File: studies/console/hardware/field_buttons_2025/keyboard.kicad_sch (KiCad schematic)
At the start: 69 parts, among them J1 Conn_02x12_Counter_Clockwise, SW1 SW_Push, SW10 SW_Push, SW11 SW_Push, SW12 SW_Push, SW13 SW_Push, SW14 SW_Push, SW15 SW_Push, SW16 SW_Push, SW17 SW_Push, SW18 SW_Push, SW19 SW_Push, SW2 SW_Push, SW20 SW_Push, SW21 SW_Push, SW22 SW_Push, SW23 SW_Push, SW24 SW_Push, SW25 SW_Push, SW26 SW_Push, SW27 SW_Push, SW28 SW_Push, SW29 SW_Push, SW3 SW_Push, SW30 SW_Push, SW31 SW_Push, SW32 SW_Push, SW4 SW_Push, SW5 SW_Push, SW6 SW_Push, SW7 SW_Push, SW8 SW_Push, SW9 SW_Push

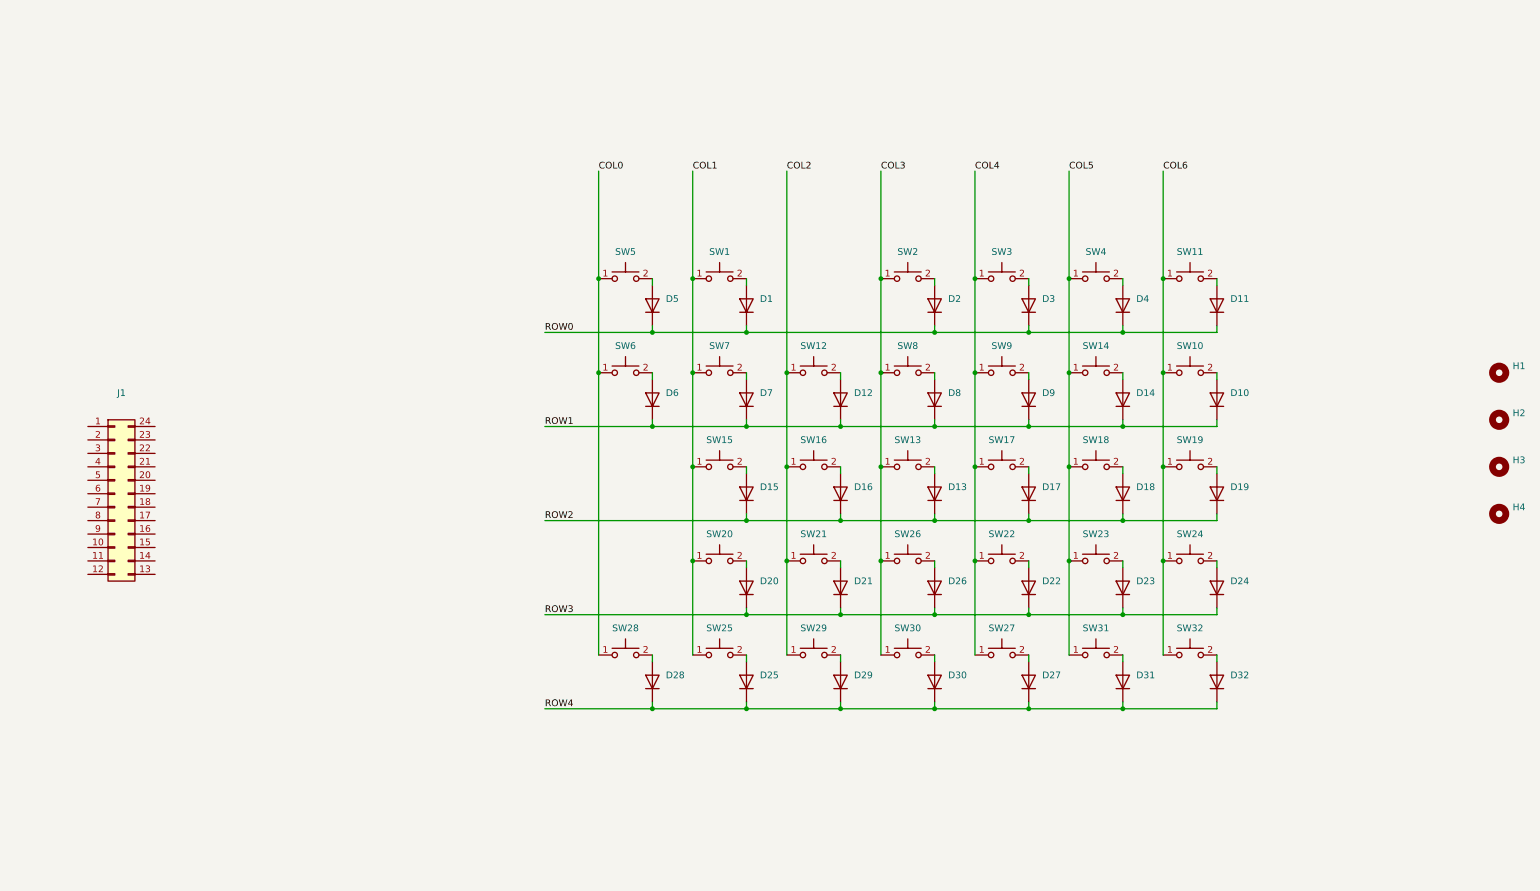
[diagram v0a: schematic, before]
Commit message: i added microcontroller tracks and code
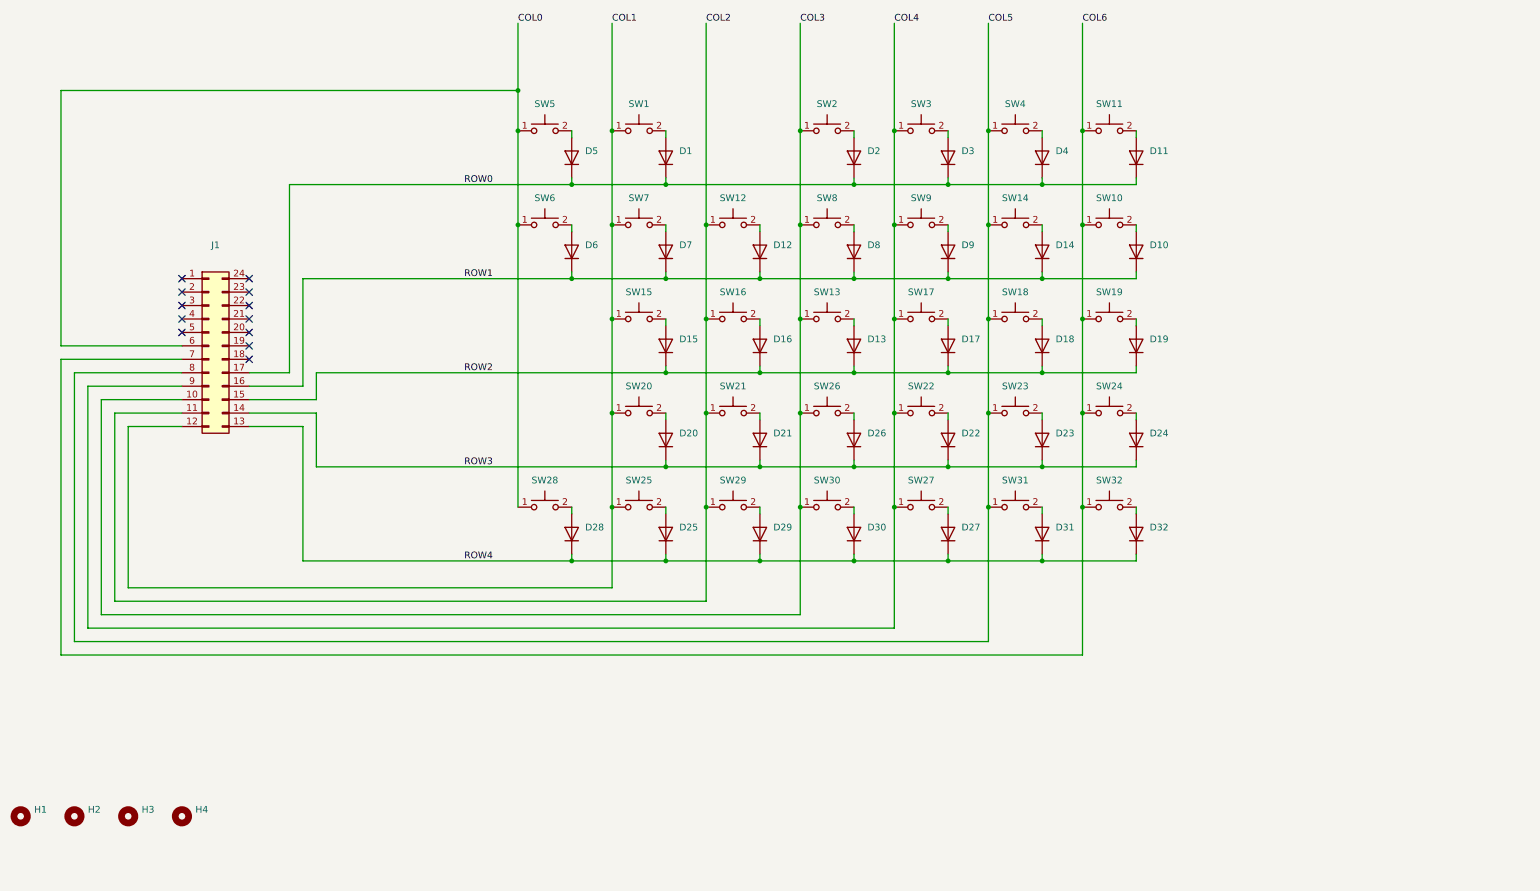
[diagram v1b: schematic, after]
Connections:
- net COL0: now also J1.6 (Pin_6)
- net COL1: now also J1.12 (Pin_12)
- net COL2: now also J1.11 (Pin_11)
- net COL3: now also J1.10 (Pin_10)
- net COL4: now also J1.9 (Pin_9)
- net COL5: now also J1.8 (Pin_8)
- net COL6: now also J1.7 (Pin_7)
- net ROW0: now also J1.17 (Pin_17)
- net ROW1: now also J1.16 (Pin_16)
- net ROW2: now also J1.15 (Pin_15)
- net ROW3: now also J1.14 (Pin_14)
- net ROW4: now also J1.13 (Pin_13)
- no-connect marks 0 -> 12
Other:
- moved on the sheet: D1, D10, D11, D12, D13, D14, D15, D16, D17, D18, D19, D2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

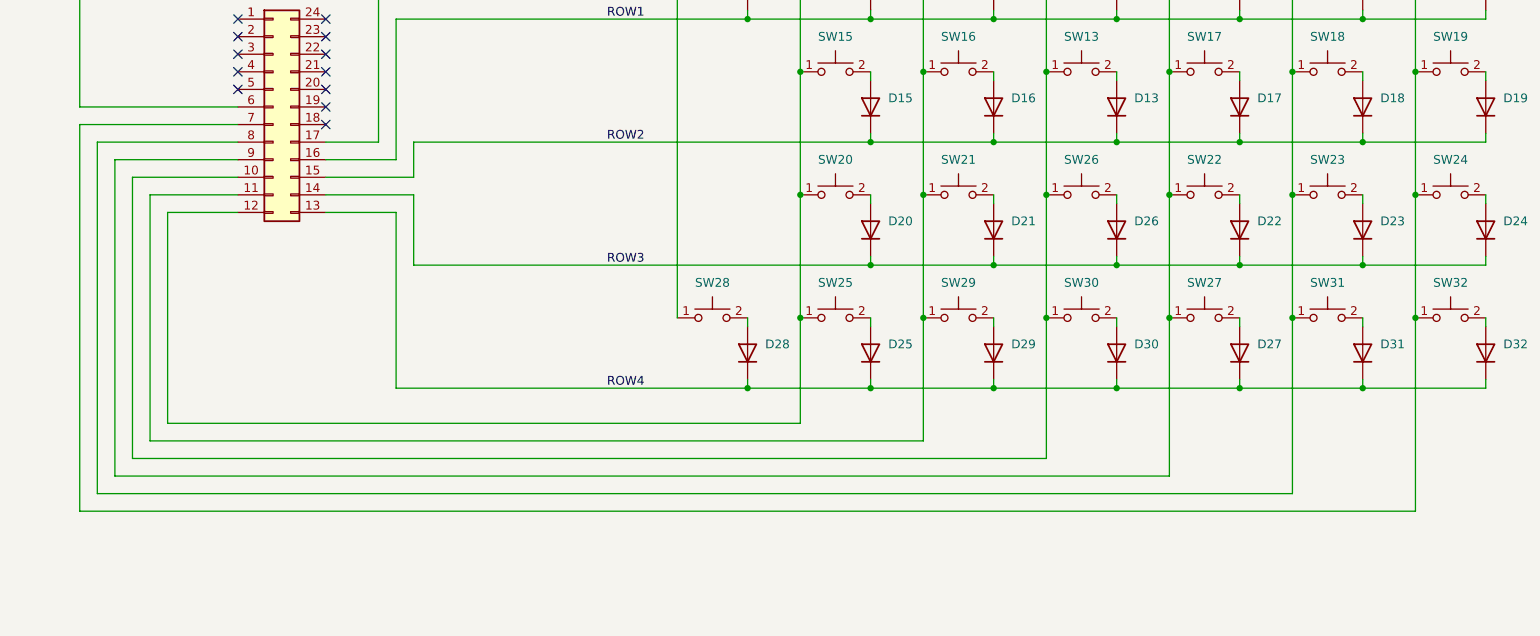
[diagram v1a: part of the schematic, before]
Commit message: add logo and strain relief
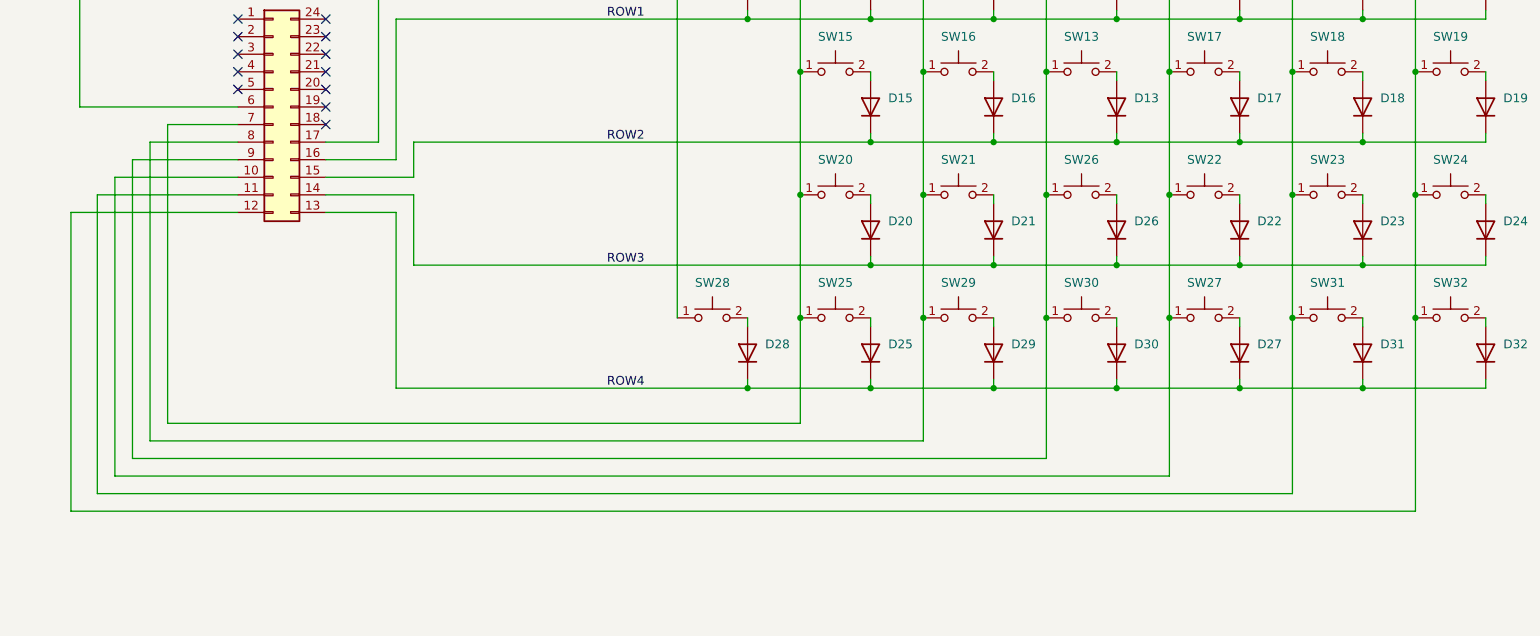
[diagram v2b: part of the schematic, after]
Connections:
- net COL1: now also J1.7 (Pin_7); no longer J1.12 (Pin_12)
- net COL2: now also J1.8 (Pin_8); no longer J1.11 (Pin_11)
- net COL3: now also J1.9 (Pin_9); no longer J1.10 (Pin_10)
- net COL4: now also J1.10 (Pin_10); no longer J1.9 (Pin_9)
- net COL5: now also J1.11 (Pin_11); no longer J1.8 (Pin_8)
- net COL6: now also J1.12 (Pin_12); no longer J1.7 (Pin_7)
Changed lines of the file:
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@@
-	(wire
-		(pts
-			(xy 55.88 104.14) (xy 55.88 139.7)
-		)
-		(stroke
-			(width 0)
-			(type default)
-		)
-	)
 	(wire
 		(pts
@@
 	(wire
 		(pts
-			(xy 50.8 99.06) (xy 68.58 99.06)
-		)
-		(stroke
-			(width 0)
-			(type default)
-		)
-	)
-	(wire
-		(pts
 			(xy 93.98 114.3) (xy 160.02 114.3)
 		)
@@
 	(wire
 		(pts
-			(xy 55.88 104.14) (xy 68.58 104.14)
+			(xy 53.34 99.06) (xy 53.34 142.24)
 		)
 		(stroke
@@
 	(wire
 		(pts
+			(xy 55.88 96.52) (xy 55.88 139.7)
+		)
+		(stroke
+			(width 0)
+			(type default)
+		)
+	)
+	(wire
+		(pts
 			(xy 195.58 130.81) (xy 195.58 132.08)
 		)
@@
 	(wire
 		(pts
+			(xy 48.26 104.14) (xy 68.58 104.14)
+		)
+		(stroke
+			(width 0)
+			(type default)
+		)
+	)
+	(wire
+		(pts
 			(xy 195.58 95.25) (xy 195.58 96.52)
 		)
@@
 	(wire
 		(pts
-			(xy 53.34 101.6) (xy 68.58 101.6)
-		)
-		(stroke
-			(width 0)
-			(type default)
-		)
-	)
-	(wire
-		(pts
 			(xy 213.36 132.08) (xy 231.14 132.08)
 		)
@@
 	(wire
 		(pts
+			(xy 68.58 99.06) (xy 53.34 99.06)
+		)
+		(stroke
+			(width 0)
+			(type default)
+		)
+	)
+	(wire
+		(pts
 			(xy 203.2 144.78) (xy 50.8 144.78)
 		)
@@
 	(wire
 		(pts
+			(xy 50.8 101.6) (xy 50.8 144.78)
+		)
+		(stroke
+			(width 0)
+			(type default)
+		)
+	)
+	(wire
+		(pts
 			(xy 203.2 68.58) (xy 203.2 86.36)
 		)
@@
 	(wire
 		(pts
-			(xy 53.34 101.6) (xy 53.34 142.24)
-		)
-		(stroke
-			(width 0)
-			(type default)
-		)
-	)
-	(wire
-		(pts
 			(xy 213.36 113.03) (xy 213.36 114.3)
 		)
@@
 	(wire
 		(pts
-			(xy 48.26 96.52) (xy 48.26 147.32)
+			(xy 48.26 104.14) (xy 48.26 147.32)
 		)
 		(stroke
@@
 	(wire
 		(pts
-			(xy 58.42 106.68) (xy 68.58 106.68)
-		)
-		(stroke
-			(width 0)
-			(type default)
-		)
-	)
-	(wire
-		(pts
 			(xy 91.44 78.74) (xy 91.44 99.06)
 		)
@@
 	(wire
 		(pts
+			(xy 58.42 93.98) (xy 68.58 93.98)
+		)
+		(stroke
+			(width 0)
+			(type default)
+		)
+	)
+	(wire
+		(pts
 			(xy 220.98 86.36) (xy 220.98 104.14)
 		)
@@
 	(wire
 		(pts
+			(xy 50.8 101.6) (xy 68.58 101.6)
+		)
+		(stroke
+			(width 0)
+			(type default)
+		)
+	)
+	(wire
+		(pts
 			(xy 185.42 86.36) (xy 185.42 104.14)
 		)
@@
 	(wire
 		(pts
+			(xy 44.45 106.68) (xy 68.58 106.68)
+		)
+		(stroke
+			(width 0)
+			(type default)
+		)
+	)
+	(wire
+		(pts
 			(xy 91.44 106.68) (xy 81.28 106.68)
 		)
@@
 	(wire
 		(pts
-			(xy 45.72 93.98) (xy 68.58 93.98)
-		)
-		(stroke
-			(width 0)
-			(type default)
-		)
-	)
-	(wire
-		(pts
 			(xy 93.98 101.6) (xy 81.28 101.6)
 		)
@@
 	(wire
 		(pts
-			(xy 58.42 137.16) (xy 58.42 106.68)
+			(xy 58.42 93.98) (xy 58.42 137.16)
 		)
 		(stroke
@@
 	(wire
 		(pts
-			(xy 50.8 99.06) (xy 50.8 144.78)
-		)
-		(stroke
-			(width 0)
-			(type default)
-		)
-	)
-	(wire
-		(pts
 			(xy 142.24 123.19) (xy 142.24 121.92)
 		)
@@
 	(wire
 		(pts
-			(xy 238.76 149.86) (xy 45.72 149.86)
+			(xy 238.76 149.86) (xy 44.45 149.86)
 		)
 		(stroke
@@
 	(wire
 		(pts
-			(xy 45.72 93.98) (xy 45.72 149.86)
+			(xy 44.45 106.68) (xy 44.45 149.86)
 		)
 		(stroke
@@
 	(wire
 		(pts
-			(xy 48.26 96.52) (xy 68.58 96.52)
-		)
-		(stroke
-			(width 0)
-			(type default)
-		)
-	)
-	(wire
-		(pts
 			(xy 213.36 130.81) (xy 213.36 132.08)
+		)
+		(stroke
+			(width 0)
+			(type default)
+		)
+	)
+	(wire
+		(pts
+			(xy 55.88 96.52) (xy 68.58 96.52)
 		)
 		(stroke
@@
 	(label "COL2"
 		(at 167.64 30.48 0)
-		(fields_autoplaced yes)
 		(effects
 			(font
@@
 	(label "ROW2"
 		(at 121.92 96.52 0)
-		(fields_autoplaced yes)
 		(effects
 			(font
@@
 	(label "ROW0"
 		(at 121.92 60.96 0)
-		(fields_autoplaced yes)
 		(effects
 			(font
@@
 	(label "COL3"
 		(at 185.42 30.48 0)
-		(fields_autoplaced yes)
 		(effects
 			(font
@@
 	(label "ROW3"
 		(at 121.92 114.3 0)
-		(fields_autoplaced yes)
 		(effects
 			(font
@@
 	(label "COL5"
 		(at 220.98 30.48 0)
-		(fields_autoplaced yes)
 		(effects
 			(font
@@
 	(label "COL0"
 		(at 132.08 30.48 0)
-		(fields_autoplaced yes)
 		(effects
 			(font
@@
 	(label "ROW4"
 		(at 121.92 132.08 0)
-		(fields_autoplaced yes)
 		(effects
 			(font
@@
 	(label "COL1"
 		(at 149.86 30.48 0)
-		(fields_autoplaced yes)
 		(effects
 			(font
@@
 	(label "COL4"
 		(at 203.2 30.48 0)
-		(fields_autoplaced yes)
 		(effects
 			(font
@@
 	(label "COL6"
 		(at 238.76 30.48 0)
-		(fields_autoplaced yes)
 		(effects
 			(font
@@
 	(label "ROW1"
 		(at 121.92 78.74 0)
-		(fields_autoplaced yes)
 		(effects
 			(font

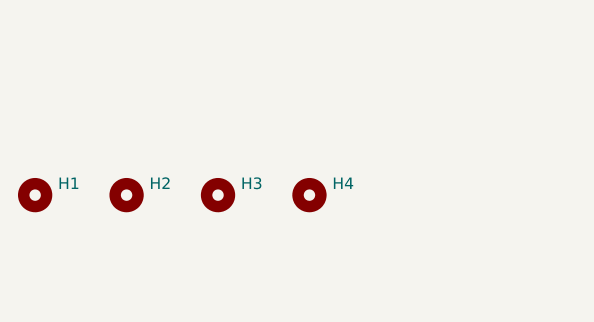
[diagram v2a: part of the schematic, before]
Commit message: use round-number inches for holes and outline
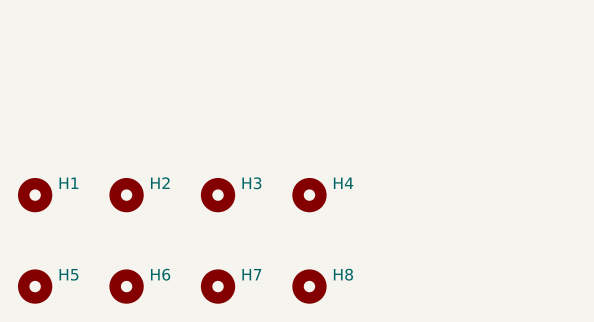
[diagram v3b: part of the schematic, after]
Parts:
- added H5: MountingHole, MountingHole:MountingHole_3.2mm_M3_ISO7380, symbol Mechanical:MountingHole
- added H6, H7, H8: MountingHole, symbol Mechanical:MountingHole
